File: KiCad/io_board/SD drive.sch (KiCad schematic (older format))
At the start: 7 parts, among them J3 SD_Card, U12 AMS1117-3.3, U14 74HC32, U7 EPM240M100, X2 10 MHz

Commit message: Worked on I/O board.
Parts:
- removed U7: EPM240M100, Package_BGA:BGA-100_6.0x6.0mm_Layout11x11_P0.5mm_Ball0.3mm_Pad0.25mm_NSMD, symbol CPLD_Altera:EPM240M100
- added C21, C22, C23, C24, C25: 100n, Capacitor_THT:C_Disc_D4.3mm_W1.9mm_P5.00mm, symbol Device:C
- added J?: JTAG, symbol Connector_Generic:Conn_02x05_Odd_Even
- added R6: 4K7, Resistor_THT:R_Axial_DIN0207_L6.3mm_D2.5mm_P7.62mm_Horizontal, symbol Device:R
- added R?: 1K, Resistor_THT:R_Axial_DIN0207_L6.3mm_D2.5mm_P7.62mm_Horizontal, symbol Device:R
- added R? (x2): 10K, Resistor_THT:R_Axial_DIN0207_L6.3mm_D2.5mm_P7.62mm_Horizontal, symbol Device:R
- added U13: SN74LVC245A, Package_SO:TSSOP-20_4.4x6.5mm_P0.65mm, symbol 74xx:74HC245
- added U15: SN74LVC8T245PWR, Package_SO:TSSOP-24_4.4x7.8mm_P0.65mm, symbol Logic_LevelTranslator:SN74AVC8T245PW
- added U7: EPM240T100, Package_QFP:LQFP-100_14x14mm_P0.5mm, symbol CPLD_Altera:EPM240T100
- C17: footprint (none) -> Capacitor_THT:CP_Radial_D5.0mm_P2.50mm
- C18: footprint (none) -> Capacitor_THT:C_Disc_D4.3mm_W1.9mm_P5.00mm
- U14: value 74HC32 -> 74HCT32; footprint (none) -> Package_SO:SOIC-14_3.9x8.7mm_P1.27mm
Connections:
- net labels added: A0_3, A1, A1_3, CPLD_CLK_3, D0, D1, D2, D3, D4, D5, D6, D7, D[0..7], SD_DI, TCK, TDI, TDO, TMS, ~CS_DRIVE_3, ~RAM_OE, ~RAM_WE, ~RD_3, ~RESET_3, ~WR_3, ~WR_BUFFER_3
- net labels removed: CS, DI, DO, SCLK
- wire segments 96 -> 178
- no-connect marks 8 -> 42
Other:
- moved on the sheet: C17, C18, U12, U14E, X2

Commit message: Working on IO board
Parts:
- added C26, C27: 100n, Capacitor_SMD:C_1206_3216Metric, symbol Device:C
- C18: footprint Capacitor_THT:C_Disc_D4.3mm_W1.9mm_P5.00mm -> Capacitor_THT:C_Disc_D3.0mm_W2.0mm_P2.50mm
- C21, C22, C23, C24, C25: footprint Capacitor_THT:C_Disc_D4.3mm_W1.9mm_P5.00mm -> Capacitor_SMD:C_1206_3216Metric
- J4: renamed from J?; footprint (none) -> Connector_IDC:IDC-Header_2x05_P2.54mm_Vertical
- gave numbers to parts that had none: 3
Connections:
- net GND: now also C26.2, C27.2
- net VCC3: now also C26.1, C27.1
- net D0_3: now reaches U15.21 (B1), U7.42 (IO1_42)
- net D1_3: now reaches U15.20 (B2), U7.43 (IO1_43/DEV_OE)
- net D2_3: now reaches U15.19 (B3), U7.44 (IO1_44/DEV_CLRn)
- net D3_3: now reaches U15.18 (B4), U7.47 (IO1_47)
- net D4_3: now reaches U15.17 (B5), U7.48 (IO1_48)
- net D5_3: now reaches U15.16 (B6), U7.49 (IO1_49)
- net D6_3: now reaches U15.15 (B7), U7.50 (IO1_50)
- net D7_3: now reaches U15.14 (B8), U7.51 (IO1_51)
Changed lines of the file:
@@
 $Descr A4 11693 8268
 encoding utf-8
-Sheet 4 7
+Sheet 4 8
 Title "Mini8086 I/O board"
 Date "2020-11-05"
@@
 F 0 "C18" H 8815 1446 50  0000 L CNN
 F 1 "100n" H 8815 1355 50  0000 L CNN
-F 2 "Capacitor_THT:C_Disc_D4.3mm_W1.9mm_P5.00mm" H 8738 1250 50  0001 C CNN
+F 2 "Capacitor_THT:C_Disc_D3.0mm_W2.0mm_P2.50mm" H 8738 1250 50  0001 C CNN
 F 3 "~" H 8700 1400 50  0001 C CNN
 	1    8700 1400
@@
 F 0 "C21" H 9215 1446 50  0000 L CNN
 F 1 "100n" H 9215 1355 50  0000 L CNN
-F 2 "Capacitor_THT:C_Disc_D4.3mm_W1.9mm_P5.00mm" H 9138 1250 50  0001 C CNN
+F 2 "Capacitor_SMD:C_1206_3216Metric" H 9138 1250 50  0001 C CNN
 F 3 "~" H 9100 1400 50  0001 C CNN
 	1    9100 1400
@@
 F 0 "C22" H 9615 1446 50  0000 L CNN
 F 1 "100n" H 9615 1355 50  0000 L CNN
-F 2 "Capacitor_THT:C_Disc_D4.3mm_W1.9mm_P5.00mm" H 9538 1250 50  0001 C CNN
+F 2 "Capacitor_SMD:C_1206_3216Metric" H 9538 1250 50  0001 C CNN
 F 3 "~" H 9500 1400 50  0001 C CNN
 	1    9500 1400
@@
 F 0 "C23" H 10015 1446 50  0000 L CNN
 F 1 "100n" H 10015 1355 50  0000 L CNN
-F 2 "Capacitor_THT:C_Disc_D4.3mm_W1.9mm_P5.00mm" H 9938 1250 50  0001 C CNN
+F 2 "Capacitor_SMD:C_1206_3216Metric" H 9938 1250 50  0001 C CNN
 F 3 "~" H 9900 1400 50  0001 C CNN
 	1    9900 1400
@@
 F 0 "C24" H 8815 2196 50  0000 L CNN
 F 1 "100n" H 8815 2105 50  0000 L CNN
-F 2 "Capacitor_THT:C_Disc_D4.3mm_W1.9mm_P5.00mm" H 8738 2000 50  0001 C CNN
+F 2 "Capacitor_SMD:C_1206_3216Metric" H 8738 2000 50  0001 C CNN
 F 3 "~" H 8700 2150 50  0001 C CNN
 	1    8700 2150
@@
 F 0 "C25" H 9215 2196 50  0000 L CNN
 F 1 "100n" H 9215 2105 50  0000 L CNN
-F 2 "Capacitor_THT:C_Disc_D4.3mm_W1.9mm_P5.00mm" H 9138 2000 50  0001 C CNN
+F 2 "Capacitor_SMD:C_1206_3216Metric" H 9138 2000 50  0001 C CNN
 F 3 "~" H 9100 2150 50  0001 C CNN
 	1    9100 2150
@@
 $EndComp
 Wire Wire Line
-	9100 1900 10300 1900
+	9100 1900 9500 1900
 Wire Wire Line
 	10300 1900 10300 2350
@@
 D7
 $Comp
-L Connector_Generic:Conn_02x05_Odd_Even J?
+L Connector_Generic:Conn_02x05_Odd_Even J4
 U 1 1 5FA5638C
 P 4000 7100
-F 0 "J?" H 4050 7517 50  0000 C CNN
+F 0 "J4" H 4050 7517 50  0000 C CNN
 F 1 "JTAG" H 4050 7426 50  0000 C CNN
-F 2 "" H 4000 7100 50  0001 C CNN
+F 2 "Connector_IDC:IDC-Header_2x05_P2.54mm_Vertical" H 4000 7100 50  0001 C CNN
 F 3 "~" H 4000 7100 50  0001 C CNN
 	1    4000 7100
@@
 	4600 7000 4600 6900
 $Comp
-L power:GND #PWR?
+L power:GND #PWR0103
 U 1 1 5FA70809
 P 4450 7400
-F 0 "#PWR?" H 4450 7150 50  0001 C CNN
+F 0 "#PWR0103" H 4450 7150 50  0001 C CNN
 F 1 "GND" H 4455 7227 50  0000 C CNN
 F 2 "" H 4450 7400 50  0001 C CNN
@@
 $EndComp
 $Comp
-L power:VCC #PWR?
+L power:VCC #PWR0104
 U 1 1 5FA70A6F
 P 4600 6900
-F 0 "#PWR?" H 4600 6750 50  0001 C CNN
+F 0 "#PWR0104" H 4600 6750 50  0001 C CNN
 F 1 "VCC" H 4615 7073 50  0000 C CNN
 F 2 "" H 4600 6900 50  0001 C CNN
@@
 	2850 5900 3950 5900
 $Comp
-L Device:R R?
+L Device:R R7
 U 1 1 5FAE490F
 P 3350 6400
-F 0 "R?" H 3420 6446 50  0000 L CNN
+F 0 "R7" H 3420 6446 50  0000 L CNN
 F 1 "1K" H 3420 6355 50  0000 L CNN
 F 2 "Resistor_THT:R_Axial_DIN0207_L6.3mm_D2.5mm_P7.62mm_Horizontal" V 3280 6400 50  0001 C CNN
@@
 $EndComp
 $Comp
-L Device:R R?
+L Device:R R8
 U 1 1 5FAFD2DA
 P 3650 6400
-F 0 "R?" H 3720 6446 50  0000 L CNN
+F 0 "R8" H 3720 6446 50  0000 L CNN
 F 1 "10K" H 3720 6355 50  0000 L CNN
 F 2 "Resistor_THT:R_Axial_DIN0207_L6.3mm_D2.5mm_P7.62mm_Horizontal" V 3580 6400 50  0001 C CNN
@@
 $EndComp
 $Comp
-L Device:R R?
+L Device:R R9
 U 1 1 5FAFD51F
 P 3950 6400
-F 0 "R?" H 4020 6446 50  0000 L CNN
+F 0 "R9" H 4020 6446 50  0000 L CNN
 F 1 "10K" H 4020 6355 50  0000 L CNN
 F 2 "Resistor_THT:R_Axial_DIN0207_L6.3mm_D2.5mm_P7.62mm_Horizontal" V 3880 6400 50  0001 C CNN
@@
 	3350 6000 3150 6000
 $Comp
-L power:GND #PWR?
+L power:GND #PWR0105
 U 1 1 5FB27EA1
 P 3350 6650
-F 0 "#PWR?" H 3350 6400 50  0001 C CNN
+F 0 "#PWR0105" H 3350 6400 50  0001 C CNN
 F 1 "GND" H 3355 6477 50  0000 C CNN
 F 2 "" H 3350 6650 50  0001 C CNN
@@
 Wire Wire Line
 	3950 6250 3950 5900
+Connection ~ 3950 5900
+Wire Wire Line
+	3950 5900 4200 5900
+$Comp
+L Device:C C26
+U 1 1 5FAF831F
+P 9500 2150
+F 0 "C26" H 9615 2196 50  0000 L CNN
+F 1 "100n" H 9615 2105 50  0000 L CNN
+F 2 "Capacitor_SMD:C_1206_3216Metric" H 9538 2000 50  0001 C CNN
+F 3 "~" H 9500 2150 50  0001 C CNN
+	1    9500 2150
+	1    0    0    -1
+$EndComp
+$Comp
+L Device:C C27
+U 1 1 5FAF84EE
+P 9900 2150
+F 0 "C27" H 10015 2196 50  0000 L CNN
+F 1 "100n" H 10015 2105 50  0000 L CNN
+F 2 "Capacitor_SMD:C_1206_3216Metric" H 9938 2000 50  0001 C CNN
+F 3 "~" H 9900 2150 50  0001 C CNN
+	1    9900 2150
+	1    0    0    -1
+$EndComp
+Wire Wire Line
+	9100 2400 9500 2400
+Wire Wire Line
+	9500 2400 9500 2300
+Wire Wire Line
+	9900 2400 9900 2300
+Wire Wire Line
+	9500 2400 9900 2400
+Connection ~ 9500 2400
+Wire Wire Line
+	9500 2000 9500 1900
+Connection ~ 9500 1900
+Wire Wire Line
+	9500 1900 9900 1900
+Wire Wire Line
+	9900 2000 9900 1900
+Connection ~ 9900 1900
+Wire Wire Line
+	9900 1900 10300 1900
+Text Label 3200 5000 0    50   ~ 0
+D0_3
+Text Label 3200 5100 0    50   ~ 0
+D1_3
+Text Label 3200 5200 0    50   ~ 0
+D2_3
+Text Label 3200 5300 0    50   ~ 0
+D3_3
+Text Label 3200 5400 0    50   ~ 0
+D4_3
+Text Label 3200 5500 0    50   ~ 0
+D5_3
+Text Label 3200 5600 0    50   ~ 0
+D6_3
+Text Label 3200 5700 0    50   ~ 0
+D7_3
 Wire Bus Line
 	1200 2350 1200 2500
@@
 Wire Bus Line
 	1100 4850 1100 5600
-Connection ~ 3950 5900
-Wire Wire Line
-	3950 5900 4200 5900
 $EndSCHEMATC

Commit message: Worked on I/O board.
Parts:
- added C28: 10n, Capacitor_THT:C_Disc_D4.3mm_W1.9mm_P5.00mm, symbol Device:C
- added C29: 100n, Capacitor_SMD:C_1206_3216Metric, symbol Device:C
- R6, R8, R9: footprint Resistor_THT:R_Axial_DIN0207_L6.3mm_D2.5mm_P7.62mm_Horizontal -> Resistor_THT:R_Axial_DIN0207_L6.3mm_D2.5mm_P2.54mm_Vertical
- R7: value 1K -> 2K2; footprint Resistor_THT:R_Axial_DIN0207_L6.3mm_D2.5mm_P7.62mm_Horizontal -> Resistor_THT:R_Axial_DIN0207_L6.3mm_D2.5mm_P2.54mm_Vertical
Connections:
- net CARD_DET: now also C28.1
- net GND: now also C28.2, C29.2; no longer R8.2, R9.2
- net VCC: now also R8.2, R9.2
- net VCC3: now also C29.1
- no-connect marks 42 -> 45
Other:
- moved on the sheet: C17, C18, C21, C22, C23, C24, C25, C26, C27, J3, J4, R6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

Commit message: Continued work on I/O board.
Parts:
- added C37: 100n, Capacitor_SMD:C_1206_3216Metric, symbol Device:C
- C18: footprint Capacitor_THT:C_Disc_D3.0mm_W2.0mm_P2.50mm -> Capacitor_SMD:C_1206_3216Metric
- C28: footprint Capacitor_THT:C_Disc_D4.3mm_W1.9mm_P5.00mm -> Capacitor_SMD:C_1206_3216Metric
- R6, R7, R8, R9: footprint Resistor_THT:R_Axial_DIN0207_L6.3mm_D2.5mm_P2.54mm_Vertical -> Resistor_SMD:R_1206_3216Metric
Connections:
- net GND: now also C37.2
- net VCC: no longer J4.4 (Pin_4), R8.2, R9.2
- net VCC3: now also J4.4 (Pin_4), R8.2, R9.2, C37.1
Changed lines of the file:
@@
 F 0 "C18" H 8565 1446 50  0000 L CNN
 F 1 "100n" H 8565 1355 50  0000 L CNN
-F 2 "Capacitor_THT:C_Disc_D3.0mm_W2.0mm_P2.50mm" H 8488 1250 50  0001 C CNN
+F 2 "Capacitor_SMD:C_1206_3216Metric" H 8488 1250 50  0001 C CNN
 F 3 "~" H 8450 1400 50  0001 C CNN
 	1    8450 1400
@@
 	5600 1600 5500 1600
 Connection ~ 5500 1600
-$Comp
-L CPLD_Altera:EPM240T100 U7
-U 1 1 5FA7828B
-P 5200 4100
-F 0 "U7" H 5200 4150 50  0000 C CNN
-F 1 "EPM240T100" H 5200 4000 50  0000 C CNN
-F 2 "Package_QFP:LQFP-100_14x14mm_P0.5mm" H 5600 1750 50  0001 L CNN
-F 3 "https://www.altera.com/content/dam/altera-www/global/en_US/pdfs/literature/hb/max2/max2_mii5v1.pdf" H 5200 4100 50  0001 C CNN
-	1    5200 4100
-	1    0    0    -1
-$EndComp
-Wire Wire Line
-	5400 6500 5500 6500
-Connection ~ 5500 6500
-Wire Wire Line
-	5400 6500 5300 6500
-Connection ~ 5400 6500
-Connection ~ 4900 6500
-Wire Wire Line
-	4900 6500 4800 6500
-Connection ~ 5000 6500
-Wire Wire Line
-	5000 6500 4900 6500
-Connection ~ 5100 6500
-Wire Wire Line
-	5100 6500 5000 6500
-Connection ~ 5200 6500
-Wire Wire Line
-	5200 6500 5100 6500
-Connection ~ 5300 6500
-Wire Wire Line
-	5300 6500 5200 6500
 Entry Wire Line
 	1300 2600 1200 2500
@@
 F 0 "R6" H 10120 2546 50  0000 L CNN
 F 1 "4K7" H 10120 2455 50  0000 L CNN
-F 2 "Resistor_THT:R_Axial_DIN0207_L6.3mm_D2.5mm_P2.54mm_Vertical" V 9980 2500 50  0001 C CNN
+F 2 "Resistor_SMD:R_1206_3216Metric" V 9980 2500 50  0001 C CNN
 F 3 "~" H 10050 2500 50  0001 C CNN
 	1    10050 2500
@@
 	1    0    0    -1
 $EndComp
-$Comp
-L power:VCC #PWR0104
-U 1 1 5FA70A6F
-P 4600 6600
-F 0 "#PWR0104" H 4600 6450 50  0001 C CNN
-F 1 "VCC" H 4615 6773 50  0000 C CNN
-F 2 "" H 4600 6600 50  0001 C CNN
-F 3 "" H 4600 6600 50  0001 C CNN
-	1    4600 6600
-	1    0    0    -1
-$EndComp
 Wire Wire Line
 	4200 6000 3350 6000
@@
 F 0 "R7" H 3420 6396 50  0000 L CNN
 F 1 "2K2" H 3420 6305 50  0000 L CNN
-F 2 "Resistor_THT:R_Axial_DIN0207_L6.3mm_D2.5mm_P2.54mm_Vertical" V 3280 6350 50  0001 C CNN
+F 2 "Resistor_SMD:R_1206_3216Metric" V 3280 6350 50  0001 C CNN
 F 3 "~" H 3350 6350 50  0001 C CNN
 	1    3350 6350
@@
 F 0 "R8" H 3720 6396 50  0000 L CNN
 F 1 "10K" H 3720 6305 50  0000 L CNN
-F 2 "Resistor_THT:R_Axial_DIN0207_L6.3mm_D2.5mm_P2.54mm_Vertical" V 3580 6350 50  0001 C CNN
+F 2 "Resistor_SMD:R_1206_3216Metric" V 3580 6350 50  0001 C CNN
 F 3 "~" H 3650 6350 50  0001 C CNN
 	1    3650 6350
@@
 F 0 "R9" H 4020 6396 50  0000 L CNN
 F 1 "10K" H 4020 6305 50  0000 L CNN
-F 2 "Resistor_THT:R_Axial_DIN0207_L6.3mm_D2.5mm_P2.54mm_Vertical" V 3880 6350 50  0001 C CNN
+F 2 "Resistor_SMD:R_1206_3216Metric" V 3880 6350 50  0001 C CNN
 F 3 "~" H 3950 6350 50  0001 C CNN
 	1    3950 6350
@@
 Wire Wire Line
 	3650 6700 3950 6700
-Connection ~ 4600 6700
-Wire Wire Line
-	4600 6700 4600 6600
 Connection ~ 3950 6700
 Wire Wire Line
@@
 F 0 "C28" H 10415 3346 50  0000 L CNN
 F 1 "10n" H 10415 3255 50  0000 L CNN
-F 2 "Capacitor_THT:C_Disc_D4.3mm_W1.9mm_P5.00mm" H 10338 3150 50  0001 C CNN
+F 2 "Capacitor_SMD:C_1206_3216Metric" H 10338 3150 50  0001 C CNN
 F 3 "~" H 10300 3300 50  0001 C CNN
 	1    10300 3300
@@
 $EndComp
 Wire Wire Line
-	8450 2400 8050 2400
-Wire Wire Line
 	8050 2400 8050 2300
 Connection ~ 8450 2400
@@
 Wire Wire Line
 	8050 1900 8450 1900
+Text GLabel 4700 6700 2    50   Input ~ 0
+VCC3
+Connection ~ 5500 6500
+Wire Wire Line
+	5400 6500 5500 6500
+Connection ~ 5400 6500
+Wire Wire Line
+	5400 6500 5300 6500
+Connection ~ 5300 6500
+Wire Wire Line
+	5300 6500 5200 6500
+Connection ~ 5200 6500
+Wire Wire Line
+	5200 6500 5100 6500
+Connection ~ 5100 6500
+Wire Wire Line
+	5100 6500 5000 6500
+Connection ~ 5000 6500
+Wire Wire Line
+	5000 6500 4900 6500
+Wire Wire Line
+	4900 6500 4800 6500
+Connection ~ 4900 6500
+$Comp
+L CPLD_Altera:EPM240T100 U7
+U 1 1 5FA7828B
+P 5200 4100
+F 0 "U7" H 5200 4150 50  0000 C CNN
+F 1 "EPM240T100" H 5200 4000 50  0000 C CNN
+F 2 "Package_QFP:LQFP-100_14x14mm_P0.5mm" H 5600 1750 50  0001 L CNN
+F 3 "https://www.altera.com/content/dam/altera-www/global/en_US/pdfs/literature/hb/max2/max2_mii5v1.pdf" H 5200 4100 50  0001 C CNN
+	1    5200 4100
+	1    0    0    -1
+$EndComp
+Wire Wire Line
+	4700 6700 4600 6700
+Connection ~ 4600 6700
+$Comp
+L Device:C C37
+U 1 1 5FCF4D72
+P 7500 2150
+F 0 "C37" H 7615 2196 50  0000 L CNN
+F 1 "100n" H 7615 2105 50  0000 L CNN
+F 2 "Capacitor_SMD:C_1206_3216Metric" H 7538 2000 50  0001 C CNN
+F 3 "~" H 7500 2150 50  0001 C CNN
+	1    7500 2150
+	1    0    0    -1
+$EndComp
+Wire Wire Line
+	7850 1900 7500 1900
+Wire Wire Line
+	7500 1900 7500 2000
+Wire Wire Line
+	7500 2300 7500 2400
+Wire Wire Line
+	7500 2400 8050 2400
+Connection ~ 8050 2400
+Wire Wire Line
+	8050 2400 8450 2400
 Wire Bus Line
 	1200 2350 1200 2500

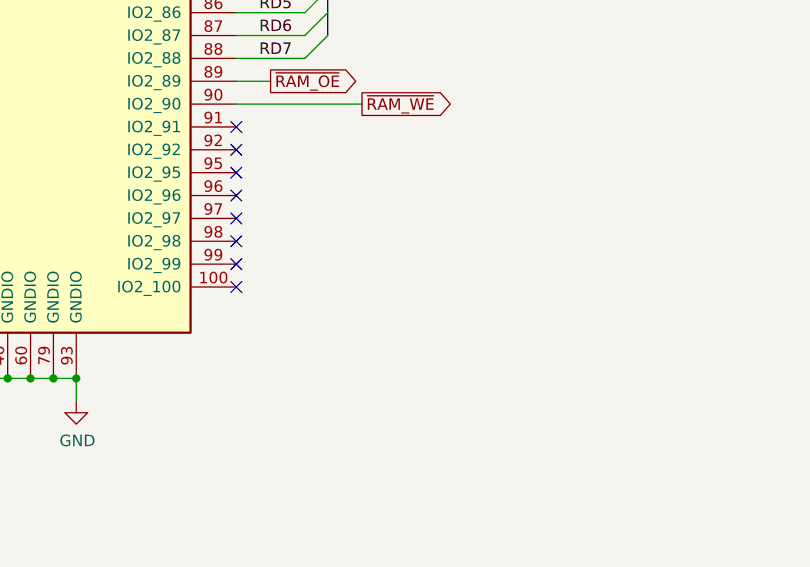
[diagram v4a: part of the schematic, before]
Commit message: Updated I/O board.
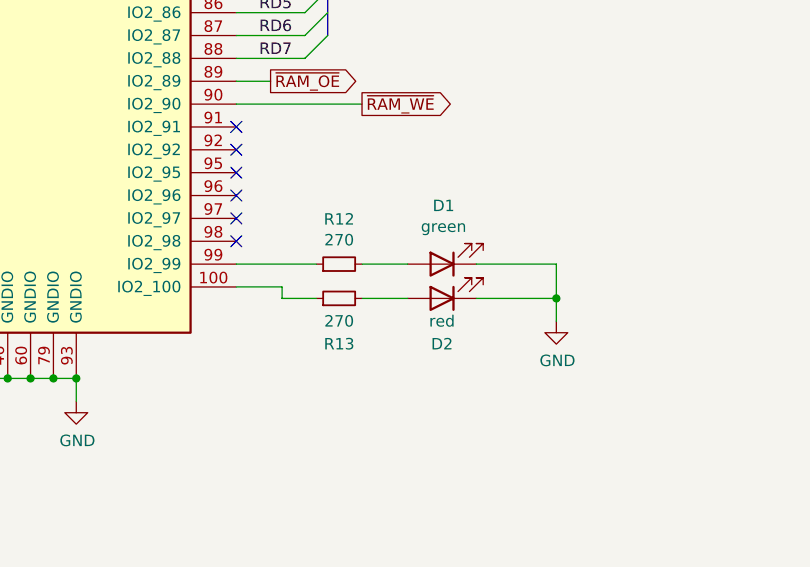
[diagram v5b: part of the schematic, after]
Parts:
- added D1: green, LED_SMD:LED_1206_3216Metric, symbol Device:LED
- added D2: red, LED_SMD:LED_1206_3216Metric, symbol Device:LED
- added R12, R13: 270, Resistor_SMD:R_1206_3216Metric, symbol Device:R_Small
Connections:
- net GND: now also D1.1 (K), D2.1 (K)
- net at U7.100 (IO2_100): now also R13.1
- net at U7.99 (IO2_99): now also R12.1
- new net: D1.2 (A), R12.2
- new net: D2.2 (A), R13.2
- no-connect marks 45 -> 43
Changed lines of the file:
@@
 NoConn ~ 6200 5800
 NoConn ~ 6200 5900
-NoConn ~ 6200 6000
-NoConn ~ 6200 6100
 NoConn ~ 4200 4900
 NoConn ~ 4200 4800
@@
 Wire Wire Line
 	8050 2400 8450 2400
+$Comp
+L Device:R_Small R12
+U 1 1 5FD5ABB9
+P 6650 6000
+F 0 "R12" V 6846 6000 50  0000 C CNN
+F 1 "270" V 6755 6000 50  0000 C CNN
+F 2 "Resistor_SMD:R_1206_3216Metric" H 6650 6000 50  0001 C CNN
+F 3 "~" H 6650 6000 50  0001 C CNN
+	1    6650 6000
+	0    -1   -1   0
+$EndComp
+$Comp
+L Device:R_Small R13
+U 1 1 5FD5B0E0
+P 6650 6150
+F 0 "R13" V 6450 6150 50  0000 C CNN
+F 1 "270" V 6550 6150 50  0000 C CNN
+F 2 "Resistor_SMD:R_1206_3216Metric" H 6650 6150 50  0001 C CNN
+F 3 "~" H 6650 6150 50  0001 C CNN
+	1    6650 6150
+	0    -1   -1   0
+$EndComp
+$Comp
+L Device:LED D1
+U 1 1 5FD77A5E
+P 7100 6000
+F 0 "D1" H 7093 5745 50  0000 C CNN
+F 1 "green" H 7093 5836 50  0000 C CNN
+F 2 "LED_SMD:LED_1206_3216Metric" H 7100 6000 50  0001 C CNN
+F 3 "~" H 7100 6000 50  0001 C CNN
+	1    7100 6000
+	-1   0    0    1
+$EndComp
+$Comp
+L Device:LED D2
+U 1 1 5FD7899C
+P 7100 6150
+F 0 "D2" H 7100 6350 50  0000 C CNN
+F 1 "red" H 7100 6250 50  0000 C CNN
+F 2 "LED_SMD:LED_1206_3216Metric" H 7100 6150 50  0001 C CNN
+F 3 "~" H 7100 6150 50  0001 C CNN
+	1    7100 6150
+	-1   0    0    1
+$EndComp
+Wire Wire Line
+	6550 6150 6400 6150
+Wire Wire Line
+	6400 6150 6400 6100
+Wire Wire Line
+	6400 6100 6200 6100
+Wire Wire Line
+	6200 6000 6550 6000
+Wire Wire Line
+	6750 6000 6950 6000
+Wire Wire Line
+	6750 6150 6950 6150
+Wire Wire Line
+	7250 6000 7600 6000
+Wire Wire Line
+	7600 6000 7600 6150
+Connection ~ 7600 6150
+Wire Wire Line
+	7600 6150 7600 6250
+Wire Wire Line
+	7250 6150 7600 6150
+$Comp
+L power:GND #PWR060
+U 1 1 5FDF2B95
+P 7600 6250
+F 0 "#PWR060" H 7600 6000 50  0001 C CNN
+F 1 "GND" H 7605 6077 50  0000 C CNN
+F 2 "" H 7600 6250 50  0001 C CNN
+F 3 "" H 7600 6250 50  0001 C CNN
+	1    7600 6250
+	1    0    0    -1
+$EndComp
 Wire Bus Line
 	1200 2350 1200 2500

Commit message: Updated I/O board
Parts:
- added C40: 100n, Capacitor_SMD:C_1206_3216Metric, symbol Device:C
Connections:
- net GND: now also C40.2
- net VCC3: now also C40.1
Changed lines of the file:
@@
 	1    0    0    -1
 $EndComp
+$Comp
+L Device:C C40
+U 1 1 5FE23D90
+P 7100 2150
+F 0 "C40" H 7215 2196 50  0000 L CNN
+F 1 "100n" H 7215 2105 50  0000 L CNN
+F 2 "Capacitor_SMD:C_1206_3216Metric" H 7138 2000 50  0001 C CNN
+F 3 "~" H 7100 2150 50  0001 C CNN
+	1    7100 2150
+	1    0    0    -1
+$EndComp
+Wire Wire Line
+	7500 2400 7100 2400
+Wire Wire Line
+	7100 2400 7100 2300
+Connection ~ 7500 2400
+Wire Wire Line
+	7100 2000 7100 1900
+Wire Wire Line
+	7100 1900 7500 1900
 Wire Bus Line
 	1200 2350 1200 2500
@@
 Wire Bus Line
 	1200 4850 1200 5600
+Connection ~ 7500 1900
 $EndSCHEMATC

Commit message: Worked on I/O board.
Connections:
- net SD_IRQ: now reaches U7.98 (IO2_98)
- no-connect marks 43 -> 42
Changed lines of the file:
@@
 NoConn ~ 6200 4300
 NoConn ~ 6200 5400
-NoConn ~ 6200 5500
 NoConn ~ 6200 5600
 NoConn ~ 6200 5700
 NoConn ~ 6200 5800
-NoConn ~ 6200 5900
 NoConn ~ 4200 4900
 NoConn ~ 4200 4800
@@
 Wire Wire Line
 	7100 1900 7500 1900
+Connection ~ 7500 1900
+Text GLabel 6750 5600 2    50   Output ~ 0
+SD_IRQ
+Wire Wire Line
+	6200 5900 6500 5900
+Wire Wire Line
+	6500 5900 6500 5600
+Wire Wire Line
+	6500 5600 6750 5600
+NoConn ~ 6200 5500
 Wire Bus Line
 	1200 2350 1200 2500
@@
 Wire Bus Line
 	1200 4850 1200 5600
-Connection ~ 7500 1900
 $EndSCHEMATC

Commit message: Updated I/O board
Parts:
- removed X2: 10 MHz, Oscillator:Oscillator_DIP-14, symbol Oscillator:CXO_DIP14
- added C10: 47µ, Capacitor_SMD:CP_Elec_5x5.4, symbol Device:CP
- added R15: 2K2, Resistor_SMD:R_1206_3216Metric, symbol Device:R
- added R16, R17, R18, R19: 4K7, Resistor_SMD:R_1206_3216Metric, symbol Device:R
- added X2: 20 MHz, Oscillator:Oscillator_SMD_Abracon_ASV-4Pin_7.0x5.1mm, symbol Oscillator:ASV-xxxMHz
- C17: footprint Capacitor_THT:CP_Radial_D5.0mm_P2.50mm -> Capacitor_SMD:CP_Elec_5x5.4
- R12, R13: value 270 -> 100
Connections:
- net CPLD_CLK: now also U7.12 (IO1_12/GCLK0), X2.3 (OUT); no longer U13.9 (A7)
- net D0_3: now also U7.41 (IO1_41); no longer U7.42 (IO1_42)
- net D1_3: now also U7.42 (IO1_42); no longer U7.43 (IO1_43/DEV_OE)
- net D2_3: now also U7.43 (IO1_43/DEV_OE); no longer U7.44 (IO1_44/DEV_CLRn)
- net GND: now also C10.2, X2.2 (GND)
- net SD_CS: now also U7.70 (IO2_70), R17.2; no longer U7.64 (IO2_64/GCLK3)
- net VCC: now also R15.1
- net VCC3: now also C10.1, R16.1, R17.1, R18.1, R19.1, X2.1 (EN), X2.4 (Vdd)
- net ~CS_DRIVE: no longer U15.22 (~OE)
- net ~RESET_3: now also U7.44 (IO1_44/DEV_CLRn); no longer U7.2 (IO1_2)
- net at J3.8 (DAT1): now also R18.2
- net at J3.9 (DAT2): now also R19.2
- net LD_RD: now reaches R13.1, U7.100 (IO2_100)
- net ~D_EN_3: now reaches U7.40 (IO1_40)
- net MOSI: now reaches U7.71 (IO2_71)
- net MOSI: now also J3.2 (CMD)
- net SCLK: now reaches U7.72 (IO2_72)
- net SCLK: now also J3.5 (CLK)
- net MISO: now reaches U7.73 (IO2_73)
- net MISO: now also J3.7 (DAT0), R16.2
- net LD_GN: now reaches R12.1, U7.99 (IO2_99)
- net CPLD_CLK_3: no longer names the net of U13.11 (B7)
- net CPLD_CLK_3: no longer U7.12 (IO1_12/GCLK0)
- net SD_DI: no longer names the net of U7.66 (IO2_66)
- net SD_DI: no longer J3.2 (CMD)
- net SD_DO: no longer names the net of U7.68 (IO2_68)
- net SD_DO: no longer J3.7 (DAT0)
- net SD_SCLK: no longer names the net of U7.67 (IO2_67)
- net SD_SCLK: no longer J3.5 (CLK)
- net ~WR_BUFFER renamed ~CS_BUFFER
- net ~WR_BUFFER_3 renamed ~CS_BUFFER_3
- new net ~D_EN: R15.2, U15.22 (~OE)
- no-connect marks 42 -> 41
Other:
- note added: "low ESR"
- moved on the sheet: C17, C18, C21, C22, C23, C28, D1, D2, J3, R12, R13, R6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
